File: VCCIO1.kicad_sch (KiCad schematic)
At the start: 19 parts, among them U2 rv1126/rv1109, U3 MTFC4GACAJCN

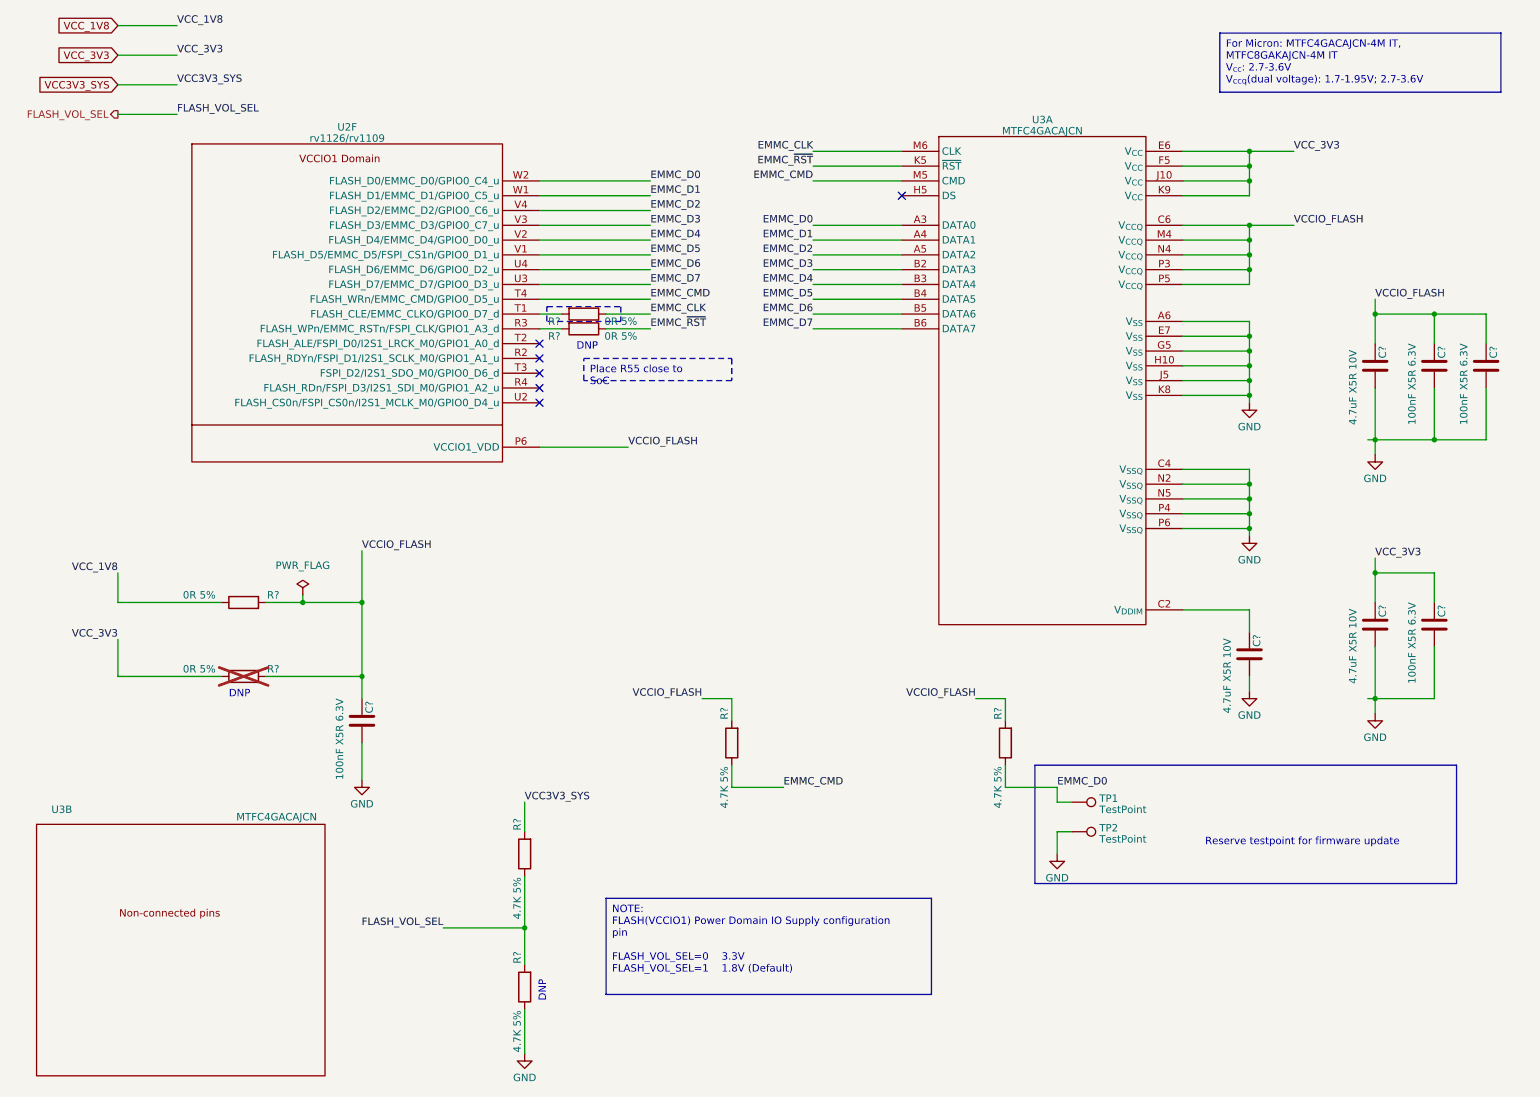
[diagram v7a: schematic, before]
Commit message: replaced Leaf specified symbols with unified iotpi symbols
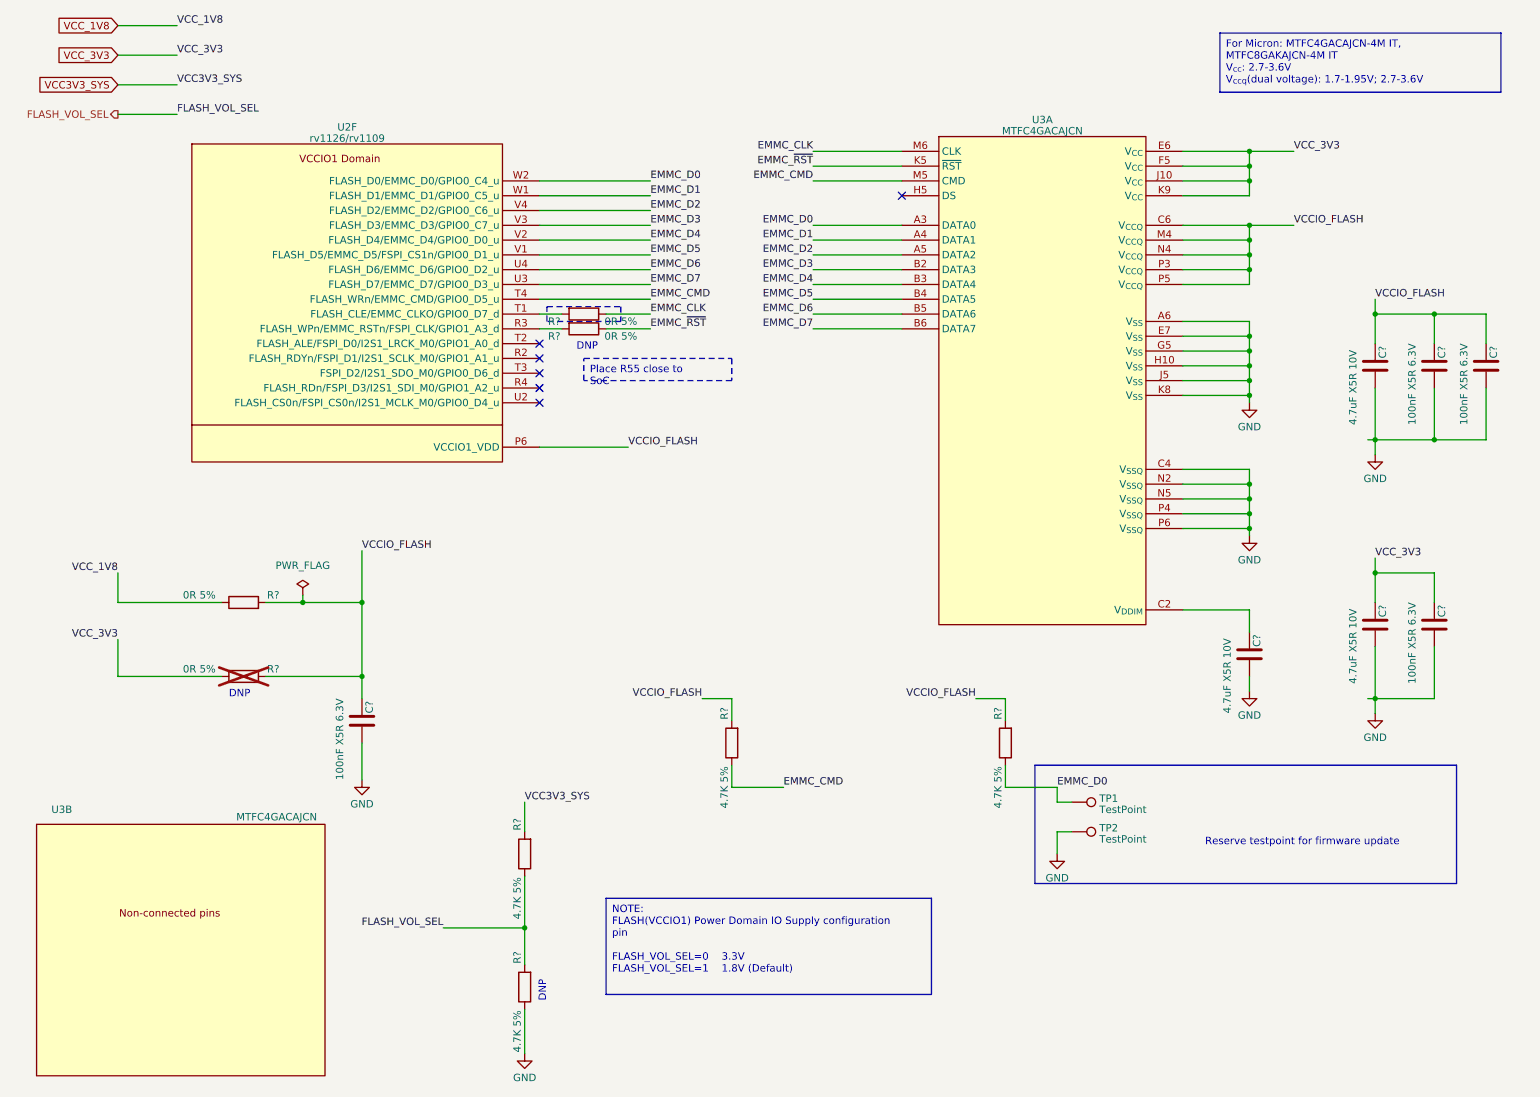
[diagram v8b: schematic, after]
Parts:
- U2: symbol CPU_Rockchip:rv1126_rv1109 -> IotPi_CPU_Rockchip:rv1126_rv1109
- U3: symbol Memory_eMMC:MTFC4GACAJCN -> IotPi_Memory_eMMC:MTFC4GACAJCN
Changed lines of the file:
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@@
     )
   )
-  (symbol (lib_id "Memory_eMMC:MTFC4GACAJCN") (at 38.1 171.45 0) (unit 2)
+  (symbol (lib_id "IotPi_Memory_eMMC:MTFC4GACAJCN") (at 38.1 171.45 0) (unit 2)
     (in_bom yes) (on_board yes) (dnp no)
     (property "Reference" "U3" (at 17.78 149.86 0)
@@
     )
     (property "Datasheet" "" (at 29.21 166.37 0)
+      (effects (font (size 1.27 1.27)) hide)
+    )
+    (property "LCSC" "" (at 38.1 171.45 0)
+      (effects (font (size 1.27 1.27)) hide)
+    )
+    (property "Description" "" (at 38.1 171.45 0)
+      (effects (font (size 1.27 1.27)) hide)
+    )
+    (property "Vendor" "" (at 38.1 171.45 0)
       (effects (font (size 1.27 1.27)) hide)
     )
@@
     )
   )
-  (symbol (lib_id "Memory_eMMC:MTFC4GACAJCN") (at 187.96 53.34 0) (unit 1)
+  (symbol (lib_id "IotPi_Memory_eMMC:MTFC4GACAJCN") (at 187.96 53.34 0) (unit 1)
     (in_bom yes) (on_board yes) (dnp no) (fields_autoplaced)
     (property "Reference" "U3" (at 187.96 31.4071 0)
@@
     )
     (property "Datasheet" "" (at 179.07 48.26 0)
+      (effects (font (size 1.27 1.27)) hide)
+    )
+    (property "LCSC" "" (at 187.96 53.34 0)
+      (effects (font (size 1.27 1.27)) hide)
+    )
+    (property "Description" "" (at 187.96 53.34 0)
+      (effects (font (size 1.27 1.27)) hide)
+    )
+    (property "Vendor" "" (at 187.96 53.34 0)
       (effects (font (size 1.27 1.27)) hide)
     )
@@
     )
   )
-  (symbol (lib_id "CPU_Rockchip:rv1126_rv1109") (at 68.58 59.69 0) (unit 6)
+  (symbol (lib_id "IotPi_CPU_Rockchip:rv1126_rv1109") (at 68.58 59.69 0) (unit 6)
     (in_bom yes) (on_board yes) (dnp no) (fields_autoplaced)
     (property "Reference" "U2" (at 68.58 32.6771 0)
@@
       (effects (font (size 1.27 1.27)))
     )
-    (property "Footprint" "Rockchip_SoC:Rockchip_RV1126_FCCSP409LD_14.0x14.0mm" (at 100.33 86.36 0)
-      (effects (font (size 1.27 1.27)) hide)
-    )
-    (property "Datasheet" "" (at 100.33 86.36 0)
-      (effects (font (size 1.27 1.27)) hide)
-    )
+    (property "Footprint" "Rockchip_SoC:Rockchip_RV1126_FCCSP409LD_14.0x14.0mm" (at 100.33 106.68 0)
+      (effects (font (size 1.27 1.27)) hide)
+    )
+    (property "Datasheet" "" (at 100.33 106.68 0)
+      (effects (font (size 1.27 1.27)) hide)
+    )
